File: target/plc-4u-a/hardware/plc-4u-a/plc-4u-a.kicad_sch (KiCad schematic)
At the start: 41 parts, among them J1 Screw_Terminal_01x02, J10 Screw_Terminal_01x02, J11 Conn_01x04_Male, J12 Conn_01x04_Male, J2 Screw_Terminal_01x02, J3 Screw_Terminal_01x02, J4 Screw_Terminal_01x02, J5 Screw_Terminal_01x02, J6 Screw_Terminal_01x02, J7 Screw_Terminal_01x02, J8 Screw_Terminal_01x02, J9 Screw_Terminal_01x02, Q1 IRF4905, Q2 IRF4905, Q3 IRF4905, Q4 IRF4905, U1 ATmega16-16P, U2 PC817, U3 PC817, U4 PC817, U5 PC817, Y1 Crystal

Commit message: update
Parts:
- removed J12: Conn_01x04_Male, Connector_PinHeader_2.54mm:PinHeader_1x04_P2.54mm_Vertical, symbol Connector:Conn_01x04_Male
- added J13: Valve control in, Connector_PinHeader_2.54mm:PinHeader_1x04_P2.54mm_Vertical, symbol Connector:Conn_01x04_Male
- added J14: Leak sensors, Connector_PinHeader_2.54mm:PinHeader_1x04_P2.54mm_Vertical, symbol Connector:Conn_01x04_Male
- added J15: I2C, Connector_PinHeader_2.54mm:PinHeader_1x02_P2.54mm_Vertical, symbol Connector:Conn_01x02_Male
- added J19: Valve leds, Connector_PinHeader_2.54mm:PinHeader_1x04_P2.54mm_Vertical, symbol Connector:Conn_01x04_Male
- added R13, R14, R15, R16: 820, Resistor_SMD:R_0805_2012Metric, symbol Device:R
- added R21, R22, R23, R24, R25, R26, R27, R28, R29, R30, R31: R, Resistor_SMD:R_1206_3216Metric, symbol Device:R
- added U10, U11, U12, U13, U14, U15, U16, U17, U6, U7, U8, U9: PC817, Package_DIP:DIP-4_W7.62mm, symbol Isolator:PC817
- J1, J2, J3, J4, J5: footprint TerminalBlock_Phoenix:TerminalBlock_Phoenix_MKDS-1,5-2_1x02_P5.00mm_Horizontal -> TerminalBlock_Phoenix:TerminalBlock_Phoenix_MKDS-1,5-2-5.08_1x02_P5.08mm_Horizontal
- J10: value Screw_Terminal_01x02 -> X_INS; footprint TerminalBlock_Phoenix:TerminalBlock_Phoenix_MKDS-1,5-2_1x02_P5.00mm_Horizontal -> TerminalBlock_Phoenix:TerminalBlock_Phoenix_MKDS-1,5-2-5.08_1x02_P5.08mm_Horizontal
- J11: value Conn_01x04_Male -> X Leds Btns
- J6: value Screw_Terminal_01x02 -> V_ST_HWS; footprint TerminalBlock_Phoenix:TerminalBlock_Phoenix_MKDS-1,5-2_1x02_P5.00mm_Horizontal -> TerminalBlock_Phoenix:TerminalBlock_Phoenix_MKDS-1,5-2-5.08_1x02_P5.08mm_Horizontal
- J7: value Screw_Terminal_01x02 -> V_ST_CWS; footprint TerminalBlock_Phoenix:TerminalBlock_Phoenix_MKDS-1,5-2_1x02_P5.00mm_Horizontal -> TerminalBlock_Phoenix:TerminalBlock_Phoenix_MKDS-1,5-2-5.08_1x02_P5.08mm_Horizontal
- J8: value Screw_Terminal_01x02 -> W_CT_HWS; footprint TerminalBlock_Phoenix:TerminalBlock_Phoenix_MKDS-1,5-2_1x02_P5.00mm_Horizontal -> TerminalBlock_Phoenix:TerminalBlock_Phoenix_MKDS-1,5-2-5.08_1x02_P5.08mm_Horizontal
- J9: value Screw_Terminal_01x02 -> W_CT_CWS; footprint TerminalBlock_Phoenix:TerminalBlock_Phoenix_MKDS-1,5-2_1x02_P5.00mm_Horizontal -> TerminalBlock_Phoenix:TerminalBlock_Phoenix_MKDS-1,5-2-5.08_1x02_P5.08mm_Horizontal
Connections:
- net PD2: now also J19.1 (Pin_1)
- net PD3: now also J19.2 (Pin_2)
- net VCC: now also U10.1, U11.1, U12.1, U13.1, U14.1, U15.1, U16.1, U17.1, U6.1, U7.1, U8.1, U9.1
- net VDD: now also R13.2, R14.2, R15.2, R16.2
- net X5: now reaches J8.1 (Pin_1)
- net X5: now also R22.1
- net X4: now reaches J8.2 (Pin_2)
- net X4: now also R23.1
- net SCL: now reaches U1.22 (PC0)
- net SCL: now also J15.1 (Pin_1)
- net SDA: now reaches U1.23 (PC1)
- net SDA: now also J15.2 (Pin_2)
- net PC4: now reaches U1.26 (PC4)
- net PC4: now also J13.4 (Pin_4)
- net PC5: now reaches U1.27 (PC5)
- net PC5: now also J13.3 (Pin_3)
- net PC6: now reaches U1.28 (PC6)
- net PC6: now also J13.2 (Pin_2)
- net PC7: now reaches U1.29 (PC7)
- net PC7: now also J13.1 (Pin_1)
- net PA7: now reaches U1.33 (PA7)
- net PA7: now also J14.4 (Pin_4)
- net PA6: now reaches U1.34 (PA6)
- net PA6: now also J14.3 (Pin_3)
- net PA5: now reaches U1.35 (PA5)
- net PA5: now also J14.2 (Pin_2)
- net PA4: now reaches U1.36 (PA4)
- net PA4: now also J14.1 (Pin_1)
- net PA3: now reaches U1.37 (PA3)
- net PA3: now also R13.1, U14.4
- net PA2: now reaches U1.38 (PA2)
- net PA2: now also R14.1, U15.4
- net PA1: now reaches U1.39 (PA1)
- net PA1: now also R15.1, U16.4
- net PA0: now reaches U1.40 (PA0)
- net PA0: now also R16.1, U17.4
- net X7: now reaches J9.1 (Pin_1)
- net X7: now also R31.1
- net X6: now reaches J9.2 (Pin_2)
- net X6: now also R21.1
- net X9: now reaches J10.1 (Pin_1)
- net X8: now reaches J10.2 (Pin_2)
- net X8: now also R30.1
- net X3: now reaches J7.1 (Pin_1)
- net X3: now also R24.1
- net X2: now reaches J7.2 (Pin_2)
- net X2: now also R25.1
- net X1: now reaches J6.1 (Pin_1)
- net X1: now also R26.1
- net X0: now reaches J6.2 (Pin_2)
- new net: R22.2, U12.2
- new net: R31.2, U10.2
- new net: R24.2, U14.2
- new net: R29.2, U8.2
- new net: R26.2, U16.2
- new net: R21.2, U11.2
- new net: R25.2, U15.2
- new net: R27.2, U6.2
- new net: R28.2, U7.2
- new net: R30.2, U9.2
- new net: R23.2, U13.2
- new net PD4: J19.3 (Pin_3)
- new net PD5: J19.4 (Pin_4)
- new net VSS: U10.3, U11.3, U12.3, U13.3, U14.3, U15.3, U16.3, U17.3, U6.3, U7.3, U8.3, U9.3
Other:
- added sheet Middle board (middle_board.kicad_sch)
- added sheet Top board (top_board.kicad_sch)
- note added: "FR157"
- moved on the sheet: J10, J11, J6, J7, J8, J9, U1, Y1

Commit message: update
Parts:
- removed R16: 820, Resistor_SMD:R_0805_2012Metric, symbol Device:R
- removed U17, U8: PC817, Package_DIP:DIP-4_W7.62mm, symbol Isolator:PC817
- added D10, D5, D6, D7, D8, D9: D, Diode_THT:D_DO-41_SOD81_P10.16mm_Horizontal, symbol Device:D
- added J51: U17 IN, Connector_PinHeader_2.54mm:PinHeader_1x02_P2.54mm_Vertical, symbol Connector:Conn_01x02_Male
- added J52: U8 IN, Connector_PinHeader_2.54mm:PinHeader_1x02_P2.54mm_Vertical, symbol Connector:Conn_01x02_Male
- added J55: AVR-ISP-10, Connector_IDC:IDC-Header_2x05_P2.54mm_Vertical, symbol Connector:AVR-ISP-10
- added Q5, Q6: IRF4905, Package_TO_SOT_THT:TO-220-3_Vertical, symbol Transistor_FET:IRF4905
- added R39, R55, R56, R57, R58: 820, Resistor_SMD:R_0805_2012Metric, symbol Device:R
- added R40: 8.2k, Resistor_SMD:R_0805_2012Metric, symbol Device:R
- added R41, R42: 5.1k, Resistor_SMD:R_0805_2012Metric, symbol Device:R
- added U22: MAX485E, Package_SO:SOIC-8_3.9x4.9mm_P1.27mm, symbol Interface_UART:MAX485E
- R27, R28: value R -> 820; footprint Resistor_SMD:R_1206_3216Metric -> Resistor_SMD:R_0805_2012Metric
- R29: value R -> 8.2k; footprint Resistor_SMD:R_1206_3216Metric -> Resistor_SMD:R_0805_2012Metric
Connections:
- net GND: now also U6.3, U7.3, D10.2 (A), D5.2 (A), D6.2 (A), D7.2 (A), D8.2 (A), D9.2 (A)
- net PB4: now also R3.1; no longer J11.4 (Pin_4)
- net PB5: now also R4.1; no longer J11.3 (Pin_3)
- net PB6: now also R7.1; no longer J11.2 (Pin_2)
- net PB7: now also R10.1; no longer J11.1 (Pin_1)
- net PC4: now also U10.4, R55.1
- net PC5: now also U11.4, R56.1
- net PC6: now also U12.4, R57.1
- net PC7: now also U13.4, R58.1
- net PD2: no longer J19.1 (Pin_1)
- net PD3: no longer J19.2 (Pin_2)
- net PD4: now also U1.18 (PD4); no longer J19.3 (Pin_3)
- net PD5: now also U1.19 (PD5); no longer J19.4 (Pin_4)
- net VCC: now also J51.2 (Pin_2), J52.1 (Pin_1), Q5.3 (S), Q6.3 (S), R41.2, R42.2; no longer U6.1, U7.1
- net VDD: now also U6.1, U7.1, R39.2, R55.2, R56.2, R57.2, R58.2
- net VSS: no longer U6.3, U7.3
- net X0: now also J51.1 (Pin_1)
- net X9: now also J52.2 (Pin_2)
- net Y0: now also D5.1 (K)
- net Y1: now also D6.1 (K)
- net Y2: now also D7.1 (K)
- net Y3: now also D8.1 (K)
- net PD6: now reaches U1.20 (PD6)
- net PD6: now also R27.1
- net PD7: now reaches U1.21 (PD7)
- net PD7: now also R28.1
- net PC2: now reaches U1.24 (PC2)
- net PC3: now reaches U1.25 (PC3)
- net PC3: now also U9.4, R39.1
- net at R29.2: now also Q5.1 (G), R41.1
- net at U7.4: now also R40.1
- net at R29.1: now also U6.4
- net Y4: now reaches J5.1 (Pin_1)
- net Y4: now also D9.1 (K), Q5.2 (D)
- net Y5: now reaches J5.2 (Pin_2)
- net Y5: now also D10.1 (K), Q6.2 (D)
- net PD0 renamed RXD
- net RXD: now also U22.1 (RO)
- net PD1 renamed TXD
- net TXD: now also U22.4 (DI)
- net Q0 renamed PB0
- net PB0: now also J11.1 (Pin_1); no longer R3.1
- net Q1 renamed PB1
- net PB1: now also J11.2 (Pin_2); no longer R4.1
- net Q2 renamed PB2
- net PB2: now also J11.3 (Pin_3); no longer R7.1
- net Q3 renamed PB3
- net PB3: now also J11.4 (Pin_4); no longer R10.1
- new net: Q6.1 (G), R40.2, R42.1
- new net: J55.10 (GND), J55.4 (GND), J55.6 (GND), J55.8 (GND)
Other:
- moved on the sheet: J13, J14, J15, J19, R13, R14, R15, R21, R22, R23, R24, R25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

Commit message: update
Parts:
- removed H5, H6, H7: MountingHole, MountingHole:MountingHole_3.2mm_M3, symbol Mechanical:MountingHole
- removed J51: U17 IN, Connector_PinHeader_2.54mm:PinHeader_1x02_P2.54mm_Vertical, symbol Connector:Conn_01x02_Male
- added 22pF1, 22pF2, C1: C, Capacitor_SMD:C_0805_2012Metric, symbol Device:C
- added BZ1: Buzzer, Buzzer_Beeper:Buzzer_12x9.5RM7.6, symbol Device:Buzzer
- added J53: X0, Connector_PinHeader_2.54mm:PinHeader_1x01_P2.54mm_Vertical, symbol Connector:Conn_01x01_Male
- added J58: U17 OUT, Connector_PinHeader_2.54mm:PinHeader_1x02_P2.54mm_Vertical, symbol Connector:Conn_01x02_Male
- added J59: U8 OUT, Connector_PinHeader_2.54mm:PinHeader_1x02_P2.54mm_Vertical, symbol Connector:Conn_01x02_Male
- added J61: GND, Connector_PinHeader_2.54mm:PinHeader_1x01_P2.54mm_Vertical, symbol Connector:Conn_01x01_Male
- added J63: VCC, Connector_PinHeader_2.54mm:PinHeader_1x01_P2.54mm_Vertical, symbol Connector:Conn_01x01_Male
- added J69: VDD, Connector_PinHeader_2.54mm:PinHeader_1x01_P2.54mm_Vertical, symbol Connector:Conn_01x01_Male
- added J79, J81: NC, Connector_PinHeader_2.54mm:PinHeader_1x01_P2.54mm_Vertical, symbol Connector:Conn_01x01_Male
- added JP1: Dir Control, Jumper:SolderJumper-3_P1.3mm_Bridged2Bar12_Pad1.0x1.5mm, symbol Jumper:Jumper_3_Bridged12
- added R59, R60: 820, Resistor_SMD:R_0805_2012Metric, symbol Device:R
- added R61: 1k, Resistor_SMD:R_0805_2012Metric, symbol Device:R
- J10: value X_INS -> AUX_INS
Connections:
- net GND: now also J61.1 (Pin_1)
- net PA0: now also J58.2 (Pin_2), R59.1
- net PB5: now also J55.1 (MOSI)
- net PB6: now also J55.9 (MISO)
- net PB7: now also J55.7 (SCK)
- net PC2: now also J59.2 (Pin_2), R60.1
- net SCL: now also JP1.1 (A)
- net SDA: now also BZ1.1 (-)
- net VCC: now also J63.1 (Pin_1)
- net VDD: now also J55.2 (VCC), U1.30 (AVCC), U1.32 (AREF), U22.8 (VCC), C1.1, J69.1 (Pin_1), R59.2, R60.2, R61.2
- net VSS: now also J55.10 (GND), J55.4 (GND), J55.6 (GND), J55.8 (GND), U1.11 (GND), U1.31 (GND), U22.5 (GND), 22pF1.1, 22pF2.1, BZ1.2 (+), C1.2, J58.1 (Pin_1), J59.1 (Pin_1)
- net X0: now also J53.1 (Pin_1)
- net at U1.12 (XTAL2), Y1.1: now also 22pF2.2
- net at U1.13 (XTAL1), Y1.2: now also 22pF1.2
- net RST: now reaches U1.9 (~{RESET})
- net RST: now also J55.5 (~{RST})
- net at U22.2 (~{RE}): now also U22.3 (DE), JP1.2 (C)
- net A: now reaches U22.6 (A)
- net A: now also J4.2 (Pin_2)
- net B: now reaches U22.7 (B)
- net B: now also J4.1 (Pin_1)
- new net: JP1.3 (B), R61.1

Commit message: plc-4u-a += pcb update
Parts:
- added C3: C, Capacitor_SMD:C_0805_2012Metric, symbol Device:C
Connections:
- net VDD: now also C3.1
- net VSS: now also C3.2
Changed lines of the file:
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@@
+    (stroke (width 0) (type default) (color 0 0 0 0))
+  )
+  (wire (pts (xy 207.01 88.9) (xy 207.01 95.25))
     (stroke (width 0) (type default) (color 0 0 0 0))
   )
@@
     (stroke (width 0) (type default) (color 0 0 0 0))
   )
+  (wire (pts (xy 207.01 76.2) (xy 207.01 81.28))
+    (stroke (width 0) (type default) (color 0 0 0 0))
+  )
   (wire (pts (xy 119.38 189.23) (xy 124.46 189.23))
     (stroke (width 0) (type default) (color 0 0 0 0))
@@
     (effects (font (size 1.27 1.27)) (justify left bottom))
   )
+  (label "VSS" (at 207.01 90.805 0)
+    (effects (font (size 1.27 1.27)) (justify left bottom))
+  )
   (label "RST" (at 157.48 40.64 0)
     (effects (font (size 1.27 1.27)) (justify left bottom))
@@
   )
   (label "GND" (at 50.8 68.58 0)
+    (effects (font (size 1.27 1.27)) (justify left bottom))
+  )
+  (label "VDD" (at 207.01 81.28 0)
     (effects (font (size 1.27 1.27)) (justify left bottom))
   )
@@
     (pin "2")
   )
+  (symbol (lib_id "Device:C") (at 207.01 85.09 0) (unit 1)
+    (in_bom yes) (on_board yes) (fields_autoplaced)
+    (property "Reference" "C3" (id 0) (at 210.82 83.8199 0)
+      (effects (font (size 1.27 1.27)) (justify left))
+    )
+    (property "Value" "C" (id 1) (at 210.82 86.3599 0)
+      (effects (font (size 1.27 1.27)) (justify left))
+    )
+    (property "Footprint" "Capacitor_SMD:C_0805_2012Metric" (id 2) (at 207.9752 88.9 0)
+      (effects (font (size 1.27 1.27)) hide)
+    )
+    (property "Datasheet" "~" (id 3) (at 207.01 85.09 0)
+      (effects (font (size 1.27 1.27)) hide)
+    )
+    (pin "1")
+    (pin "2")
+  )
   (symbol (lib_id "Device:R") (at 132.08 50.8 90) (unit 1)
     (in_bom yes) (on_board yes)
@@
       (reference "C2") (unit 1) (value "C_Polarized") (footprint "Capacitor_SMD:C_1812_4532Metric")
     )
+    (path "/3f598563-27e6-4200-9c15-5faa7b30e330"
+      (reference "C3") (unit 1) (value "C") (footprint "Capacitor_SMD:C_0805_2012Metric")
+    )
     (path "/1b6f69e5-ab30-4fa8-b147-99bb93679434/a17ec3d6-d5cb-48aa-be34-174beec191b3"

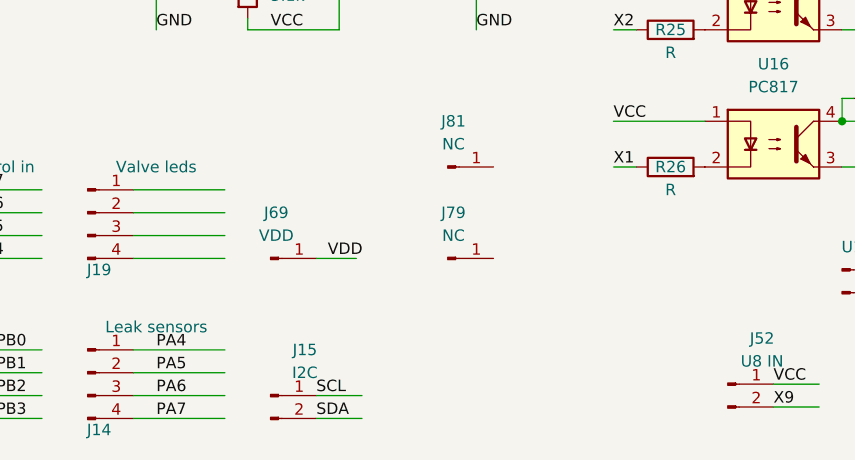
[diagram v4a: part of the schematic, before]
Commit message: plc-4u-a board += leds
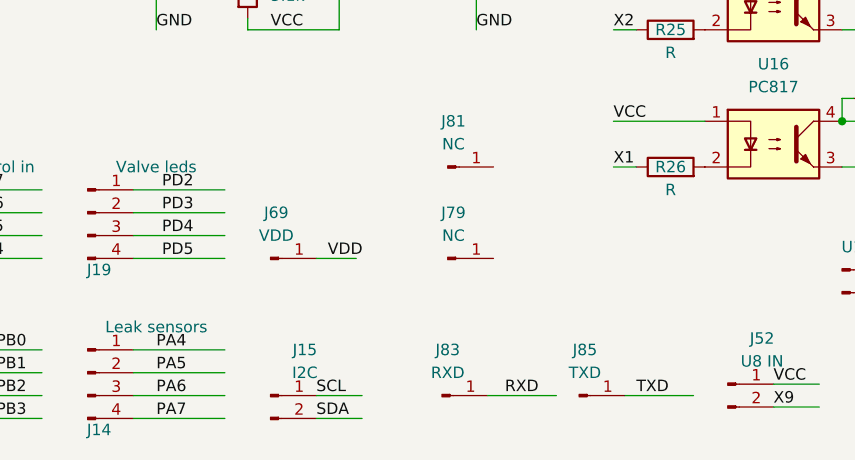
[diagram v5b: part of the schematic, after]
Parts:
- added J83: RXD, Connector_PinHeader_2.54mm:PinHeader_1x01_P2.54mm_Vertical, symbol Connector:Conn_01x01_Male
- added J85: TXD, Connector_PinHeader_2.54mm:PinHeader_1x01_P2.54mm_Vertical, symbol Connector:Conn_01x01_Male
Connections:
- net PD2: now also J19.1 (Pin_1)
- net PD3: now also J19.2 (Pin_2)
- net PD4: now also J19.3 (Pin_3)
- net PD5: now also J19.4 (Pin_4)
- net RXD: now also J83.1 (Pin_1)
- net TXD: now also J85.1 (Pin_1)
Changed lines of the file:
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@@
     (stroke (width 0) (type default) (color 0 0 0 0))
   )
+  (wire (pts (xy 87.63 190.5) (xy 95.25 190.5))
+    (stroke (width 0) (type default) (color 0 0 0 0))
+  )
   (wire (pts (xy 71.12 93.98) (xy 86.36 93.98))
     (stroke (width 0) (type default) (color 0 0 0 0))
@@
     (stroke (width 0) (type default) (color 0 0 0 0))
   )
+  (wire (pts (xy 102.87 190.5) (xy 110.49 190.5))
+    (stroke (width 0) (type default) (color 0 0 0 0))
+  )
   (wire (pts (xy 48.26 175.26) (xy 58.42 175.26))
     (stroke (width 0) (type default) (color 0 0 0 0))
@@
     (effects (font (size 1.27 1.27)) (justify left bottom))
   )
+  (label "RXD" (at 89.535 190.5 0)
+    (effects (font (size 1.27 1.27)) (justify left bottom))
+  )
   (label "RST" (at 259.715 92.71 0)
     (effects (font (size 1.27 1.27)) (justify left bottom))
@@
     (effects (font (size 1.27 1.27)) (justify left bottom))
   )
+  (label "PD4" (at 51.435 172.72 0)
+    (effects (font (size 1.27 1.27)) (justify left bottom))
+  )
   (label "X2" (at 207.01 45.72 0)
     (effects (font (size 1.27 1.27)) (justify left bottom))
@@
     (effects (font (size 1.27 1.27)) (justify left bottom))
   )
+  (label "PD2" (at 51.435 167.64 0)
+    (effects (font (size 1.27 1.27)) (justify left bottom))
+  )
   (label "PD5" (at 194.31 121.92 0)
     (effects (font (size 1.27 1.27)) (justify left bottom))
@@
     (effects (font (size 1.27 1.27)) (justify left bottom))
   )
+  (label "TXD" (at 104.14 190.5 0)
+    (effects (font (size 1.27 1.27)) (justify left bottom))
+  )
   (label "VSS" (at 135.89 73.66 0)
     (effects (font (size 1.27 1.27)) (justify left bottom))
@@
     (effects (font (size 1.27 1.27)) (justify left bottom))
   )
+  (label "PD3" (at 51.435 170.18 0)
+    (effects (font (size 1.27 1.27)) (justify left bottom))
+  )
   (label "PA6" (at 50.8 190.5 0)
     (effects (font (size 1.27 1.27)) (justify left bottom))
@@
     (effects (font (size 1.27 1.27)) (justify left bottom))
   )
+  (label "PD5" (at 51.435 175.26 0)
+    (effects (font (size 1.27 1.27)) (justify left bottom))
+  )
   (label "VDD" (at 157.48 55.88 0)
     (effects (font (size 1.27 1.27)) (justify left bottom))
@@
     (pin "4")
   )
+  (symbol (lib_id "Connector:Conn_01x01_Male") (at 82.55 190.5 0) (unit 1)
+    (in_bom yes) (on_board yes) (fields_autoplaced)
+    (property "Reference" "J83" (id 0) (at 83.185 185.42 0))
+    (property "Value" "RXD" (id 1) (at 83.185 187.96 0))
+    (property "Footprint" "Connector_PinHeader_2.54mm:PinHeader_1x01_P2.54mm_Vertical" (id 2) (at 82.55 190.5 0)
+      (effects (font (size 1.27 1.27)) hide)
+    )
+    (property "Datasheet" "~" (id 3) (at 82.55 190.5 0)
+      (effects (font (size 1.27 1.27)) hide)
+    )
+    (pin "1")
+  )
   (symbol (lib_id "Device:R") (at 107.95 165.1 90) (unit 1)
     (in_bom yes) (on_board yes)
@@
     (pin "2")
   )
+  (symbol (lib_id "Connector:Conn_01x01_Male") (at 97.79 190.5 0) (unit 1)
+    (in_bom yes) (on_board yes) (fields_autoplaced)
+    (property "Reference" "J85" (id 0) (at 98.425 185.42 0))
+    (property "Value" "TXD" (id 1) (at 98.425 187.96 0))
+    (property "Footprint" "Connector_PinHeader_2.54mm:PinHeader_1x01_P2.54mm_Vertical" (id 2) (at 97.79 190.5 0)
+      (effects (font (size 1.27 1.27)) hide)
+    )
+    (property "Datasheet" "~" (id 3) (at 97.79 190.5 0)
+      (effects (font (size 1.27 1.27)) hide)
+    )
+    (pin "1")
+  )
   (symbol (lib_id "Mechanical:MountingHole") (at 222.25 158.75 0) (unit 1)
     (in_bom yes) (on_board yes) (fields_autoplaced)
@@
       (reference "D10") (unit 1) (value "D") (footprint "Diode_THT:D_DO-41_SOD81_P10.16mm_Horizontal")
     )
+    (path "/f726a4d4-7c47-433b-b351-06d46a93f59c/e40a784d-f6ab-44db-8698-6c90e4ab4463"
+      (reference "D11") (unit 1) (value "LED") (footprint "LED_THT:LED_D3.0mm")
+    )
+    (path "/f726a4d4-7c47-433b-b351-06d46a93f59c/255b75a0-0cdd-4e7d-ace0-f4ba558c4e63"
+      (reference "D12") (unit 1) (value "LED") (footprint "LED_THT:LED_D3.0mm")
+    )
     (path "/4689d6c2-b096-4b9a-8218-9f4bb00d80c4"
       (reference "H1") (unit 1) (value "MountingHole") (footprint "MountingHole:MountingHole_3.2mm_M3")
@@
       (reference "H4") (unit 1) (value "MountingHole") (footprint "MountingHole:MountingHole_3.2mm_M3")
     )
+    (path "/f726a4d4-7c47-433b-b351-06d46a93f59c/30d13532-0e4b-4b4d-a7b2-44e8ced05919"
+      (reference "H5") (unit 1) (value "MountingHole") (footprint "MountingHole:MountingHole_3.2mm_M3")
+    )
+    (path "/f726a4d4-7c47-433b-b351-06d46a93f59c/be3dcf63-55c2-4668-b04c-aa363942fbdb"
+      (reference "H6") (unit 1) (value "MountingHole") (footprint "MountingHole:MountingHole_3.2mm_M3")
+    )
     (path "/80c21dc5-fd9f-4e61-930c-858c93a3fc9b"
       (reference "J1") (unit 1) (value "Screw_Terminal_01x02") (footprint "TerminalBlock_Phoenix:TerminalBlock_Phoenix_MKDS-1,5-2-5.08_1x02_P5.08mm_Horizontal")
@@
       (reference "J82") (unit 1) (value "NC") (footprint "Connector_PinHeader_2.54mm:PinHeader_1x01_P2.54mm_Vertical")
     )
+    (path "/8cee794c-50c7-4f25-a543-edb5bd57b631"
+      (reference "J83") (unit 1) (value "RXD") (footprint "Connector_PinHeader_2.54mm:PinHeader_1x01_P2.54mm_Vertical")
+    )
+    (path "/f726a4d4-7c47-433b-b351-06d46a93f59c/9bfcc4df-ad49-4cb9-b9fe-48fdc2d45913"
+      (reference "J84") (unit 1) (value "RXD") (footprint "Connector_PinHeader_2.54mm:PinHeader_1x01_P2.54mm_Vertical")
+    )
+    (path "/a7d9faf1-adaa-4b11-8045-25e6aab7534f"
+      (reference "J85") (unit 1) (value "TXD") (footprint "Connector_PinHeader_2.54mm:PinHeader_1x01_P2.54mm_Vertical")
+    )
+    (path "/f726a4d4-7c47-433b-b351-06d46a93f59c/0be476b3-0b73-45e9-8755-fc889c16c151"
+      (reference "J86") (unit 1) (value "TXD") (footprint "Connector_PinHeader_2.54mm:PinHeader_1x01_P2.54mm_Vertical")
+    )
     (path "/6c31e26c-d4f0-4a60-a42c-87884dfba4c7"
       (reference "JP1") (unit 1) (value "Dir Control") (footprint "Jumper:SolderJumper-3_P1.3mm_Bridged2Bar12_Pad1.0x1.5mm")
@@
       (reference "R63") (unit 1) (value "R") (footprint "Resistor_THT:R_Axial_DIN0309_L9.0mm_D3.2mm_P5.08mm_Vertical")
     )
+    (path "/f726a4d4-7c47-433b-b351-06d46a93f59c/bba97db1-ee1f-441e-b1c5-3fde0e5e41bd"
+      (reference "R64") (unit 1) (value "R") (footprint "Resistor_SMD:R_0805_2012Metric")
+    )
+    (path "/f726a4d4-7c47-433b-b351-06d46a93f59c/682bc31e-2ea6-4d97-89db-05e83a1c3d77"
+      (reference "R65") (unit 1) (value "R") (footprint "Resistor_SMD:R_0805_2012Metric")
+    )
     (path "/1b6f69e5-ab30-4fa8-b147-99bb93679434/80bfa995-b218-4c09-ab8a-2fc27238a760"
